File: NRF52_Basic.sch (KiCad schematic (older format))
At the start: 17 parts, among them J1 Conn_01x07_Male, J2 Conn_01x07_Male, J4 Conn_Coaxial, U1 nRF52832-QFxx, Y1 Crystal_GND24, Y2 Crystal

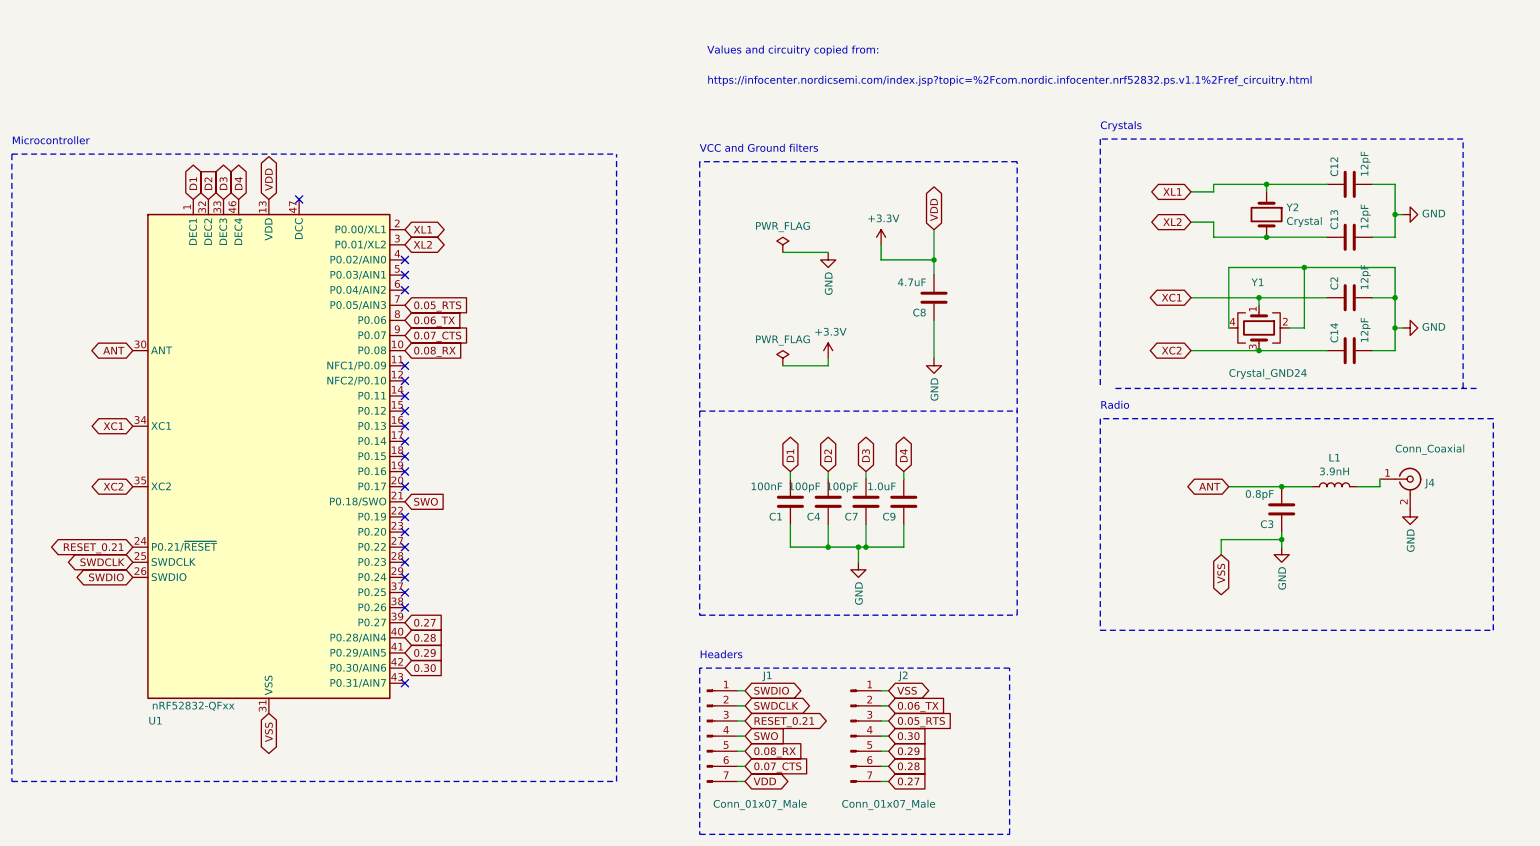
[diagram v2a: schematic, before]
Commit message: Optimized the layers and component fixtures
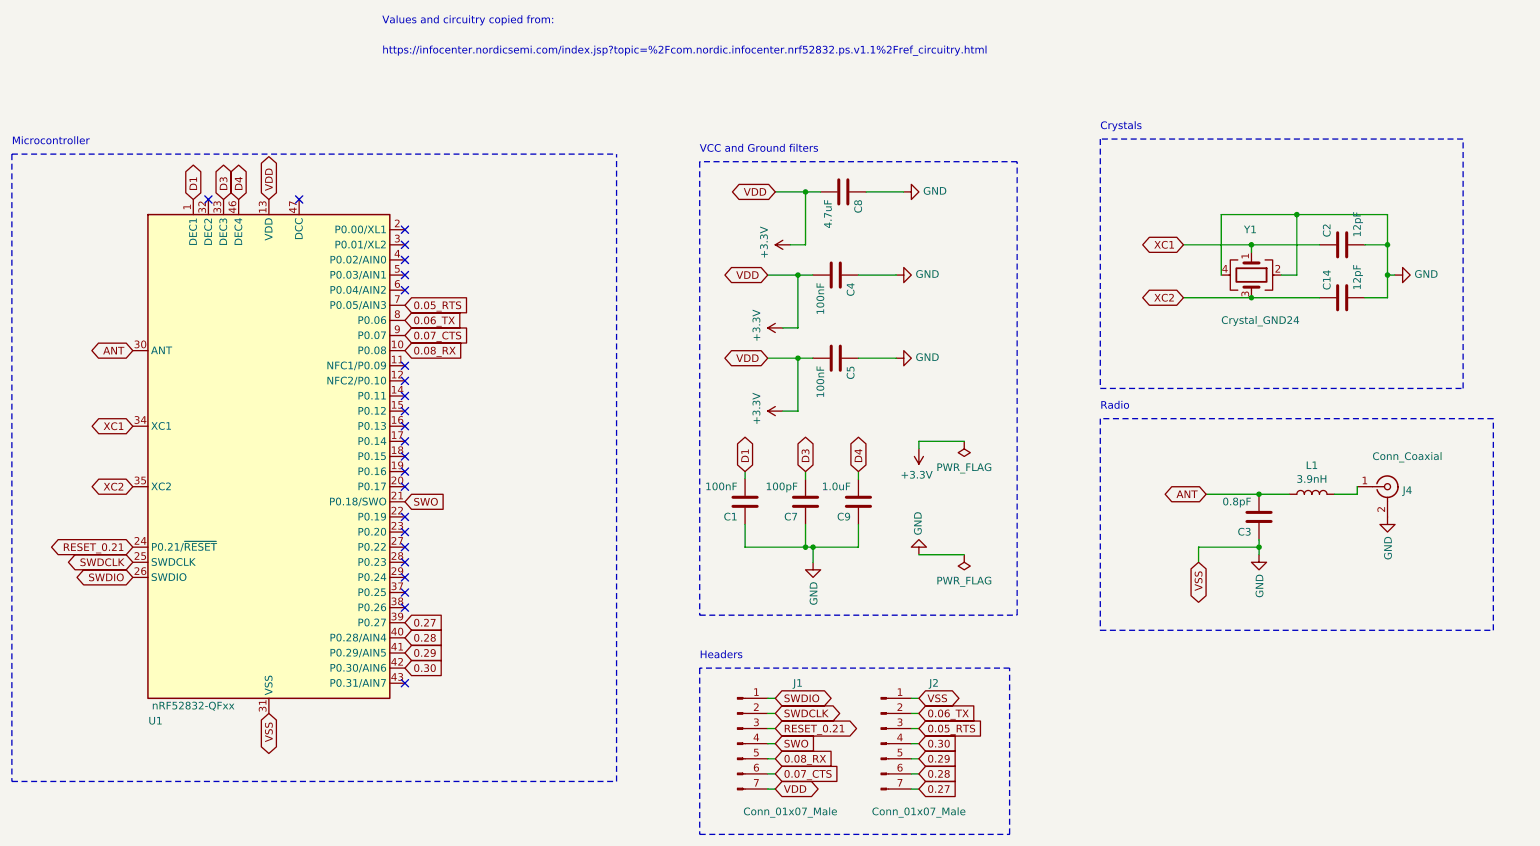
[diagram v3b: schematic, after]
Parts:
- removed C12, C13: 12pF, Capacitor_SMD:C_0201_0603Metric, symbol Device:C
- removed Y2: Crystal, Crystal:Crystal_SMD_2012-2Pin_2.0x1.2mm, symbol Device:Crystal
- added C5: 100nF, Capacitor_SMD:C_0402_1005Metric, symbol Device:C
- C1: footprint Capacitor_SMD:C_0201_0603Metric -> Capacitor_SMD:C_0402_1005Metric; LCSC Part # C14663 -> C1525
- C14, C2: footprint Capacitor_SMD:C_0201_0603Metric -> Capacitor_SMD:C_0402_1005Metric; LCSC Part # C38523 -> C1547
- C3: footprint Capacitor_SMD:C_0201_0603Metric -> Capacitor_SMD:C_0402_1005Metric; LCSC Part # C21357 -> C285068
- C4: value 100pF -> 100nF; footprint Capacitor_SMD:C_0201_0603Metric -> Capacitor_SMD:C_0402_1005Metric; LCSC Part # C14858 -> C1525
- C7: footprint Capacitor_SMD:C_0201_0603Metric -> Capacitor_SMD:C_0402_1005Metric; LCSC Part # C14858 -> C1546
- C9: footprint Capacitor_SMD:C_0402_1005Metric -> Capacitor_SMD:C_0603_1608Metric; LCSC Part # C52923 -> C15849
- L1: footprint Inductor_SMD:L_0201_0603Metric -> Inductor_SMD:L_0402_1005Metric; LCSC Part # C13818 -> C14033
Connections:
- net +3V3: now also C4.2, C5.2
- net GND: now also C5.1
- net D2: no longer names the net of U1.32 (DEC2)
- net D2: no longer C4.2
- net XL1: no longer names the net of U1.2 (P0.00/XL1)
- net XL2: no longer names the net of U1.3 (P0.01/XL2)
- no-connect marks 21 -> 24
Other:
- moved on the sheet: C1, C14, C2, C3, C7, C8, C9, J1, J2, J4, L1, Y1
